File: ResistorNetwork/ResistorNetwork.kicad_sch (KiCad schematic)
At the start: 17 parts, among them J1 Conn_01x02_Female

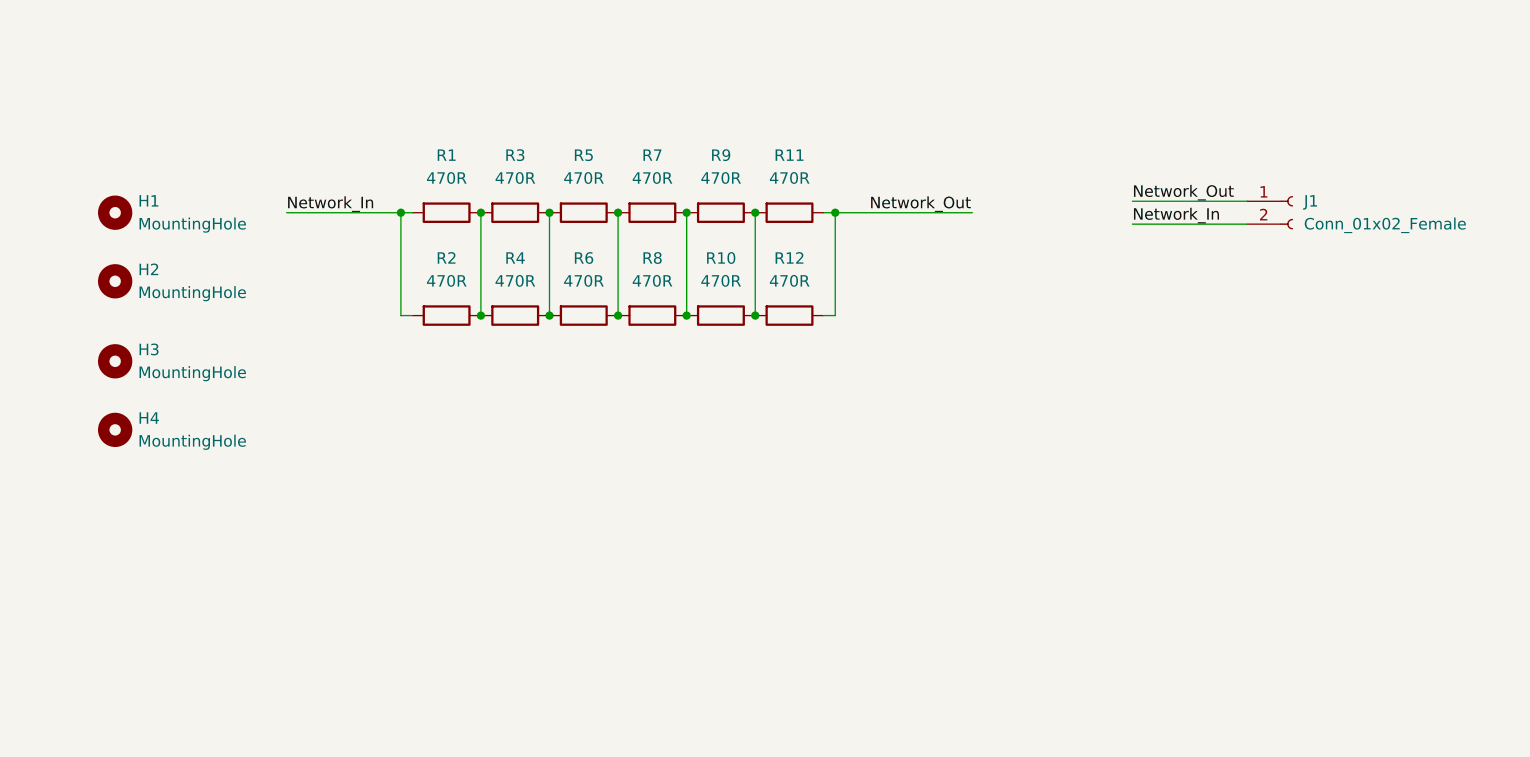
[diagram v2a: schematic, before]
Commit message: added new relay and TSMP resistors
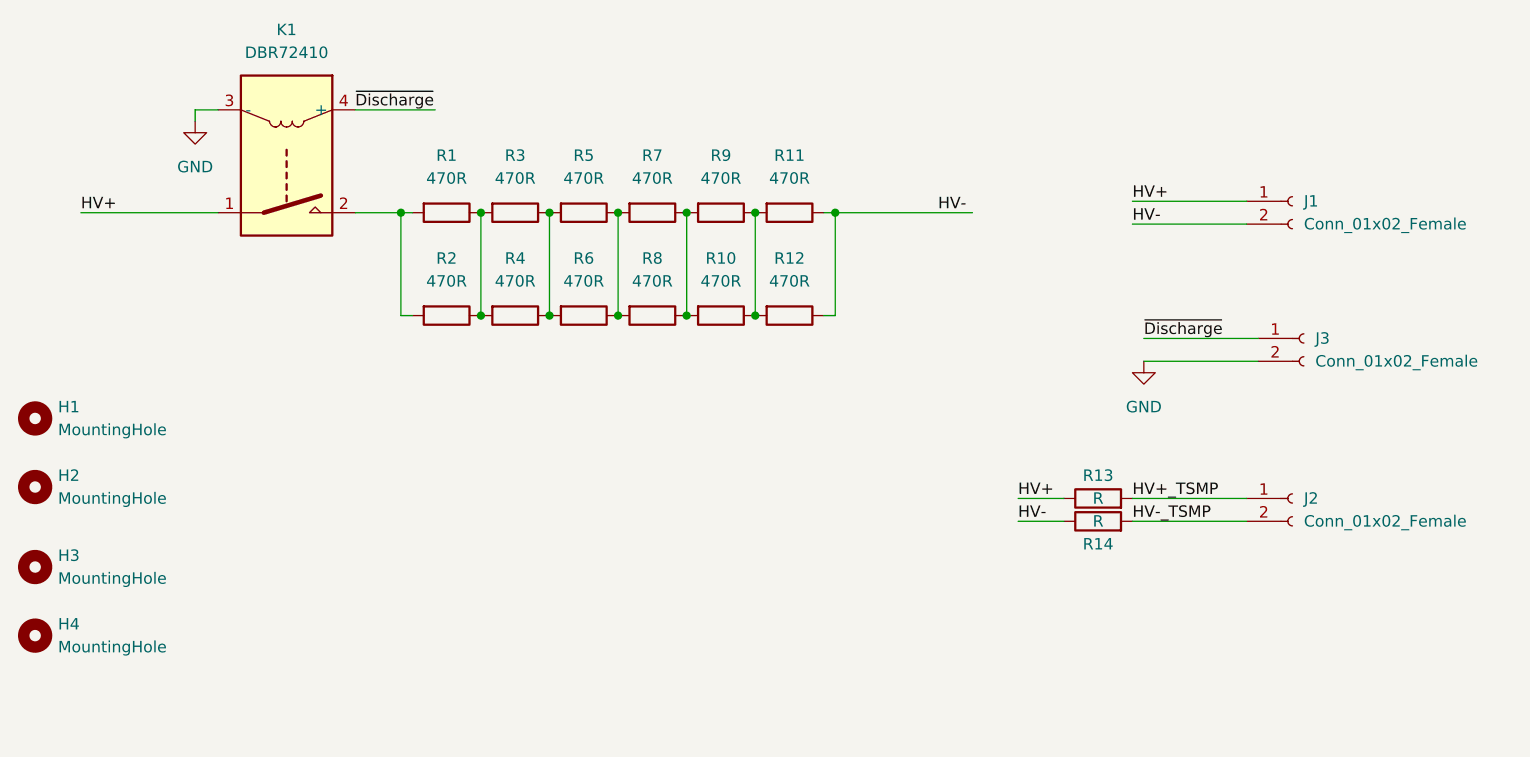
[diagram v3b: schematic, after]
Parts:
- added J2, J3: Conn_01x02_Female, Connector_Molex:Molex_Micro-Fit_3.0_43045-0200_2x01_P3.00mm_Horizontal, symbol Connector:Conn_01x02_Female
- added K1: DBR72410, Reed Relay:DBT70510U, symbol Relay:G5Q-1A
- added R13, R14: R, Resistor_SMD:3550 Resistor TE, symbol Device:R
- J1: footprint Connector_Molex:Molex_Micro-Fit_3.0_43045-0210_2x01-1MP_P3.00mm_Horizontal -> Connector_Molex:Molex_Micro-Fit_3.0_43045-0200_2x01_P3.00mm_Horizontal
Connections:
- net Network_In: no longer names the net of R1.2, R2.2
- net Network_In: now also K1.2; no longer J1.2 (Pin_2)
- net Network_Out renamed HV-
- net HV-: now also J1.2 (Pin_2), R14.1; no longer J1.1 (Pin_1)
- new net GND: J3.2 (Pin_2), K1.3 (-)
- new net HV+: J1.1 (Pin_1), K1.1, R13.1
- new net HV+_TSMP: J2.1 (Pin_1), R13.2
- new net HV-_TSMP: J2.2 (Pin_2), R14.2
- new net ~{Discharge}: J3.1 (Pin_1), K1.4 (+)
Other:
- moved on the sheet: H1, H2, H3, H4

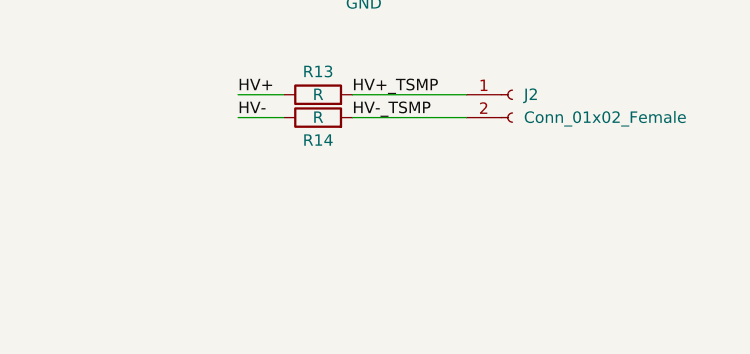
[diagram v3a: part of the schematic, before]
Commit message: added contactor fuse
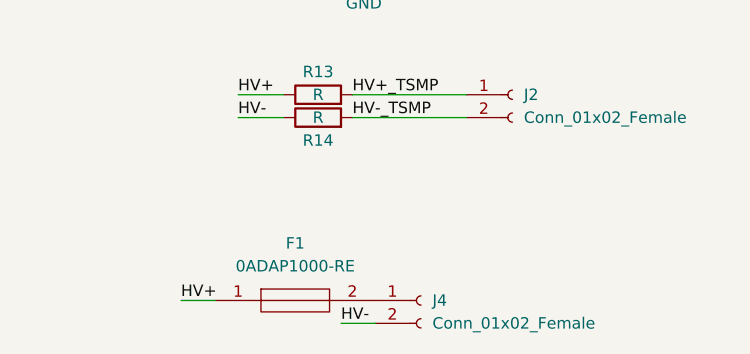
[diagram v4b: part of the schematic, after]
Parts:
- added F1: 0ADAP1000-RE, 0ADAP1000RE, symbol SamacSys_Parts:0ADAP1000-RE
- added J4: Conn_01x02_Female, Connector_Molex:Molex_Micro-Fit_3.0_43045-0200_2x01_P3.00mm_Horizontal, symbol Connector:Conn_01x02_Female
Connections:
- net HV+: now also F1.1
- net HV-: now also J4.2 (Pin_2)
- new net: F1.2, J4.1 (Pin_1)
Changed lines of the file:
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@@
   (junction (at 167.64 55.88) (diameter 0) (color 0 0 0 0)
   )
+  (wire (pts (xy 181.61 110.49) (xy 185.42 110.49))
+    (stroke (width 0) (type default) (color 0 0 0 0))
+  )
+  (wire (pts (xy 199.39 113.03) (xy 203.2 113.03))
+    (stroke (width 0) (type default) (color 0 0 0 0))
+  )
   (wire (pts (xy 187.96 87.63) (xy 193.04 87.63))
     (stroke (width 0) (type default) (color 0 0 0 0))
@@
     (effects (font (size 1.27 1.27)) (justify left bottom))
   )
+  (label "HV-" (at 199.39 113.03 0)
+    (effects (font (size 1.27 1.27)) (justify left bottom))
+  )
   (label "HV-" (at 179.07 55.88 0)
     (effects (font (size 1.27 1.27)) (justify left bottom))
@@
   )
   (label "HV-_TSMP" (at 200.66 90.17 0)
+    (effects (font (size 1.27 1.27)) (justify left bottom))
+  )
+  (label "HV+" (at 181.61 110.49 0)
     (effects (font (size 1.27 1.27)) (justify left bottom))
   )
@@
     )
     (pin "1")
+    (pin "2")
     (pin "3")
-    (pin "2")
     (pin "4")
   )
@@
     (property "Manufacturer" "Bourns" (id 6) (at 132.08 67.31 90)
       (effects (font (size 1.27 1.27)) hide)
+    )
+    (pin "1")
+    (pin "2")
+  )
+  (symbol (lib_id "SamacSys_Parts:0ADAP1000-RE") (at 185.42 110.49 0) (unit 1)
+    (in_bom yes) (on_board yes) (fields_autoplaced)
+    (property "Reference" "F1" (id 0) (at 194.31 104.14 0))
+    (property "Value" "0ADAP1000-RE" (id 1) (at 194.31 106.68 0))
+    (property "Footprint" "0ADAP1000RE" (id 2) (at 199.39 109.22 0)
+      (effects (font (size 1.27 1.27)) (justify left) hide)
+    )
+    (property "Datasheet" "https://media.digikey.com/pdf/Data%20Sheets/Bel%20Fuse%20PDFs/0ADAC_0ADAP_Series.pdf" (id 3) (at 199.39 111.76 0)
+      (effects (font (size 1.27 1.27)) (justify left) hide)
+    )
+    (property "Description" "Fuses with Leads (Through Hole) FUSE, CERAMIC TUBE 1A, 600VAC/600VDC" (id 4) (at 199.39 114.3 0)
+      (effects (font (size 1.27 1.27)) (justify left) hide)
+    )
+    (property "Height" "6.76" (id 5) (at 199.39 116.84 0)
+      (effects (font (size 1.27 1.27)) (justify left) hide)
+    )
+    (property "Manufacturer_Name" "BelFuse" (id 6) (at 199.39 119.38 0)
+      (effects (font (size 1.27 1.27)) (justify left) hide)
+    )
+    (property "Manufacturer_Part_Number" "0ADAP1000-RE" (id 7) (at 199.39 121.92 0)
+      (effects (font (size 1.27 1.27)) (justify left) hide)
+    )
+    (property "Mouser Part Number" "530-0ADAP1000-RE" (id 8) (at 199.39 124.46 0)
+      (effects (font (size 1.27 1.27)) (justify left) hide)
+    )
+    (property "Mouser Price/Stock" "https://www.mouser.co.uk/ProductDetail/Bel-Fuse/0ADAP1000-RE?qs=chTDxNqvsymIO8JrTnmTlQ%3D%3D" (id 9) (at 199.39 127 0)
+      (effects (font (size 1.27 1.27)) (justify left) hide)
+    )
+    (property "Arrow Part Number" "" (id 10) (at 199.39 129.54 0)
+      (effects (font (size 1.27 1.27)) (justify left) hide)
+    )
+    (property "Arrow Price/Stock" "" (id 11) (at 199.39 132.08 0)
+      (effects (font (size 1.27 1.27)) (justify left) hide)
+    )
+    (property "Mouser Testing Part Number" "" (id 12) (at 199.39 134.62 0)
+      (effects (font (size 1.27 1.27)) (justify left) hide)
+    )
+    (property "Mouser Testing Price/Stock" "" (id 13) (at 199.39 137.16 0)
+      (effects (font (size 1.27 1.27)) (justify left) hide)
     )
     (pin "1")
@@
     (pin "2")
   )
+  (symbol (lib_id "Connector:Conn_01x02_Female") (at 208.28 110.49 0) (unit 1)
+    (in_bom yes) (on_board yes) (fields_autoplaced)
+    (property "Reference" "J4" (id 0) (at 209.55 110.4899 0)
+      (effects (font (size 1.27 1.27)) (justify left))
+    )
+    (property "Value" "Conn_01x02_Female" (id 1) (at 209.55 113.0299 0)
+      (effects (font (size 1.27 1.27)) (justify left))
+    )
+    (property "Footprint" "Connector_Molex:Molex_Micro-Fit_3.0_43045-0200_2x01_P3.00mm_Horizontal" (id 2) (at 208.28 110.49 0)
+      (effects (font (size 1.27 1.27)) hide)
+    )
+    (property "Datasheet" "~" (id 3) (at 208.28 110.49 0)
+      (effects (font (size 1.27 1.27)) hide)
+    )
+    (pin "1")
+    (pin "2")
+  )
   (symbol (lib_id "Device:R") (at 139.7 67.31 270) (unit 1)
     (in_bom yes) (on_board yes) (fields_autoplaced)
@@
       (reference "#PWR0102") (unit 1) (value "GND") (footprint "")
     )
+    (path "/b2638a59-87bf-4634-946f-6bb5a9b6bddc"
+      (reference "F1") (unit 1) (value "0ADAP1000-RE") (footprint "0ADAP1000RE")
+    )
     (path "/5b78bd78-66b9-42dc-90f6-6ff1e98a07c3"
       (reference "H1") (unit 1) (value "MountingHole") (footprint "MountingHole:MountingHole_4.3mm_M4")
@@
       (reference "J3") (unit 1) (value "Conn_01x02_Female") (footprint "Connector_Molex:Molex_Micro-Fit_3.0_43045-0200_2x01_P3.00mm_Horizontal")
     )
+    (path "/d501a797-4011-4fc0-845b-8177ebd7f5ca"
+      (reference "J4") (unit 1) (value "Conn_01x02_Female") (footprint "Connector_Molex:Molex_Micro-Fit_3.0_43045-0200_2x01_P3.00mm_Horizontal")
+    )
     (path "/310dfc35-0a21-434e-98e5-5f78cfcb546f"
